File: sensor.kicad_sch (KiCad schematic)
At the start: 7 parts, among them U1 MAXM86161EFD+T

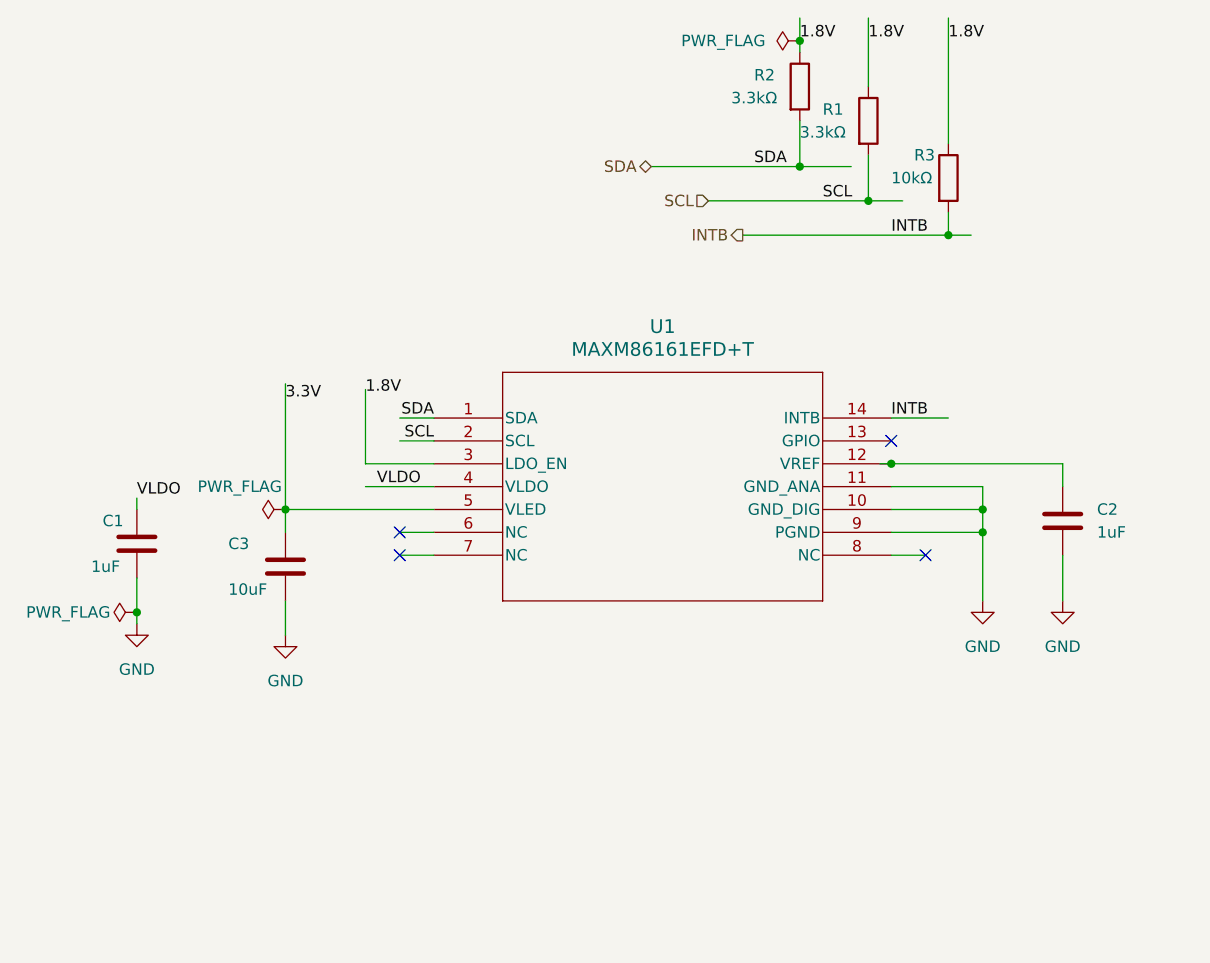
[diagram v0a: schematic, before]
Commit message: first finished schematic version of the MCU as well as sensor. starting out with schematic of the power related components
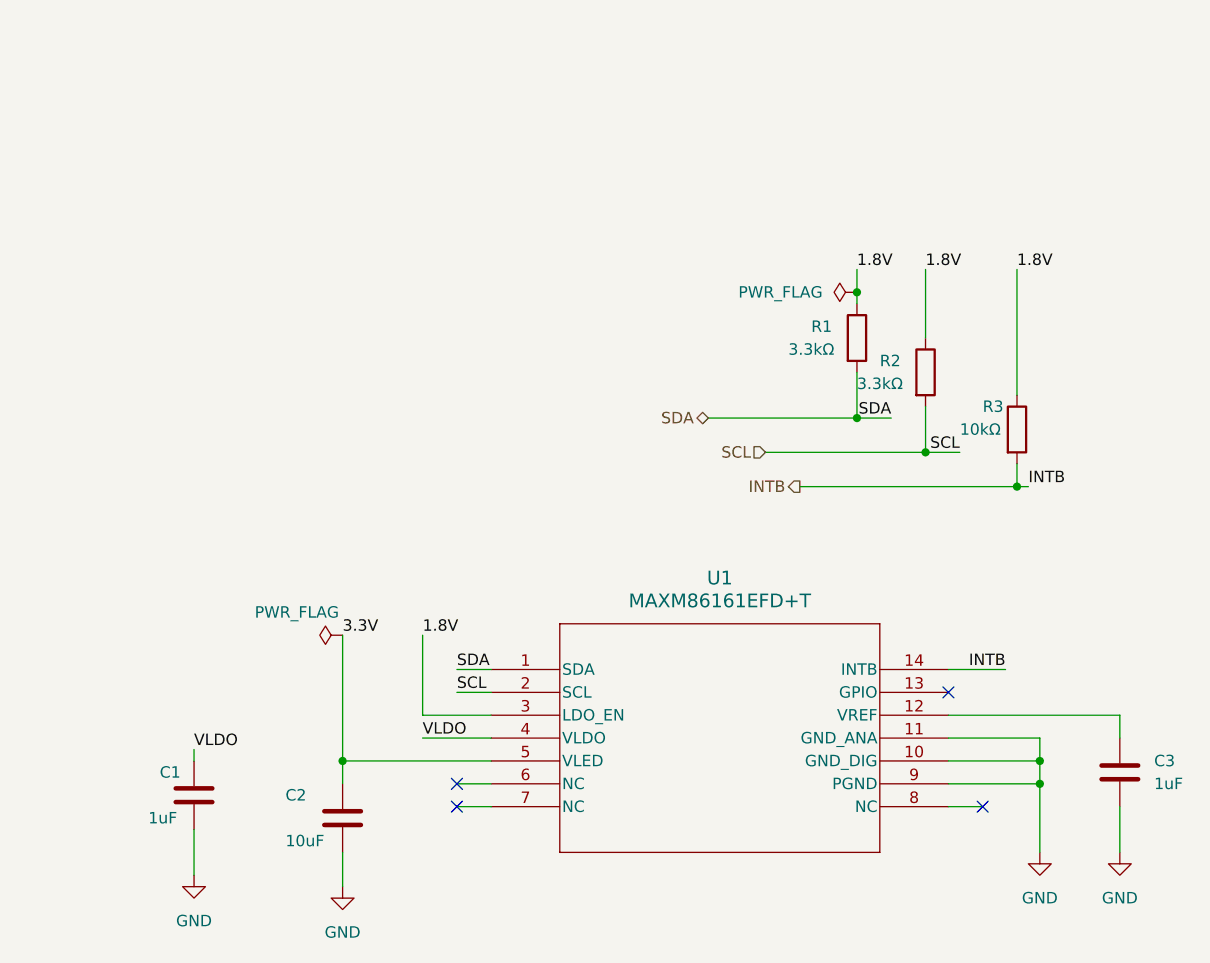
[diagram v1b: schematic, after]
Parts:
- C2: value 1uF -> 10uF
- C3: value 10uF -> 1uF
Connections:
- net 3.3V: now also C2.1; no longer C3.1
- net SCL: now also R2.2; no longer R1.2
- net SDA: now also R1.2; no longer R2.2
- net at U1.12 (VREF): now also C3.1; no longer C2.1

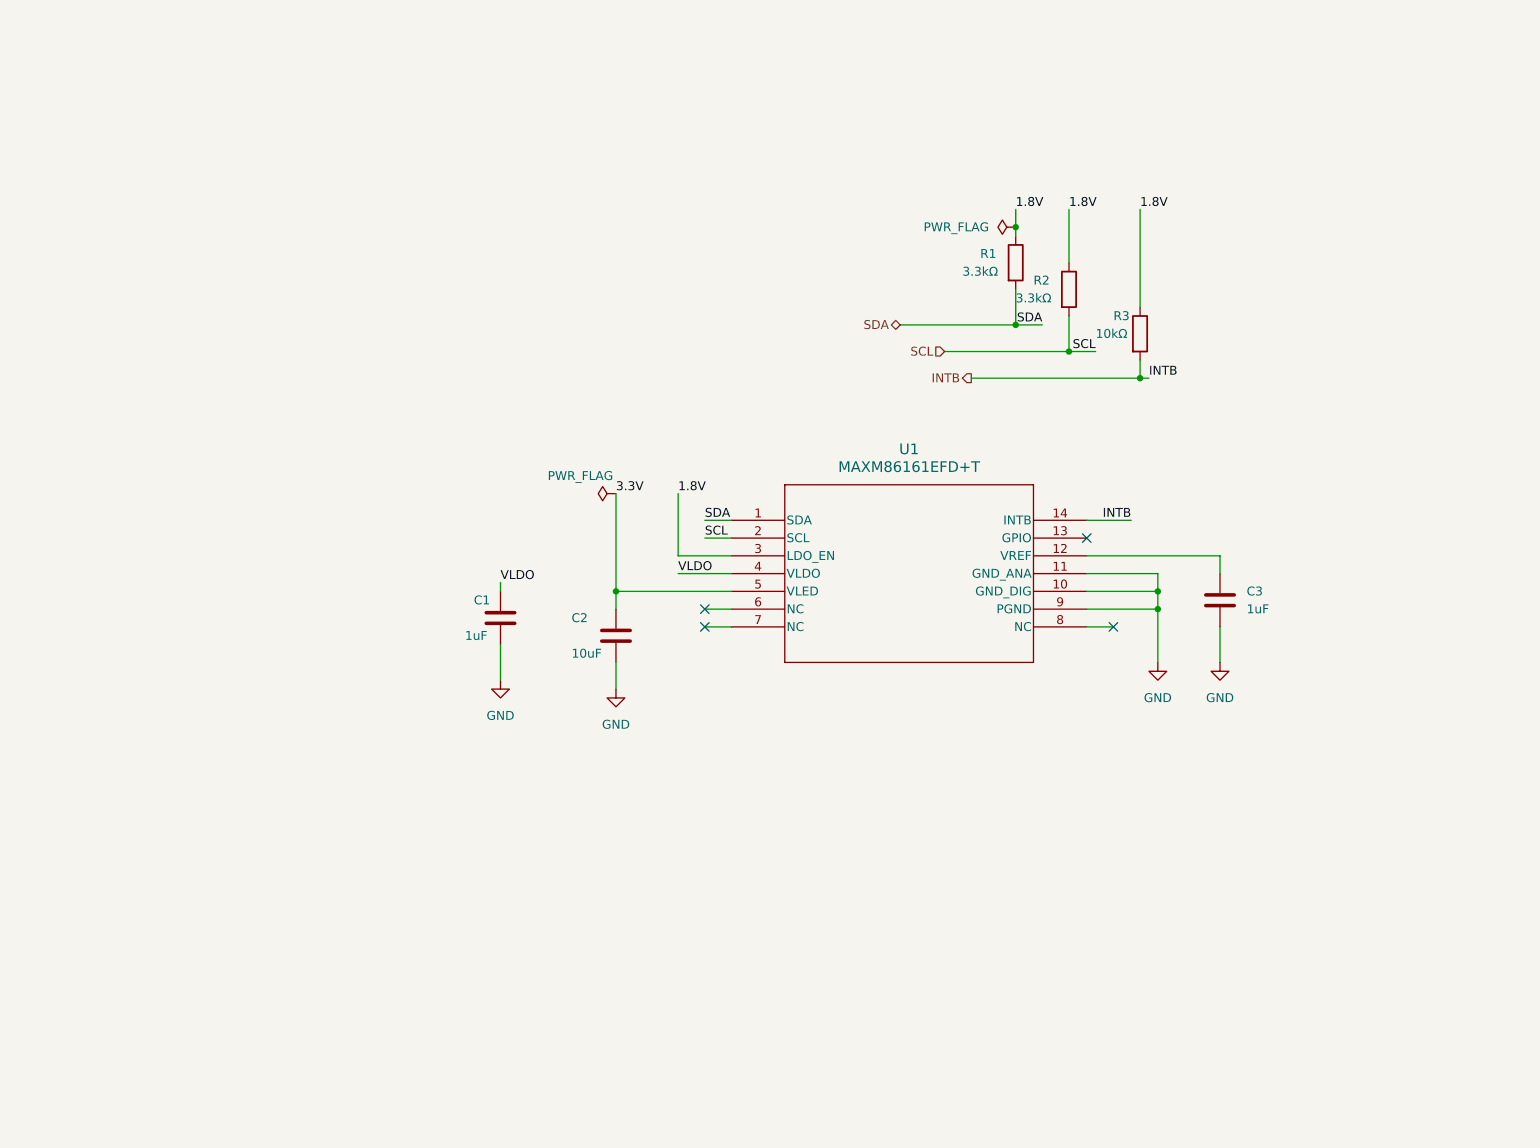
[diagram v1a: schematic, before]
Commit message: done with first version PowerSection of LoTiBloxy plus MCU plus sensor sheets. still have to add meaningfull comments to all schematic components. still have to make sure every symbol is associated to footprint. still have to perform ERC on what implemented.
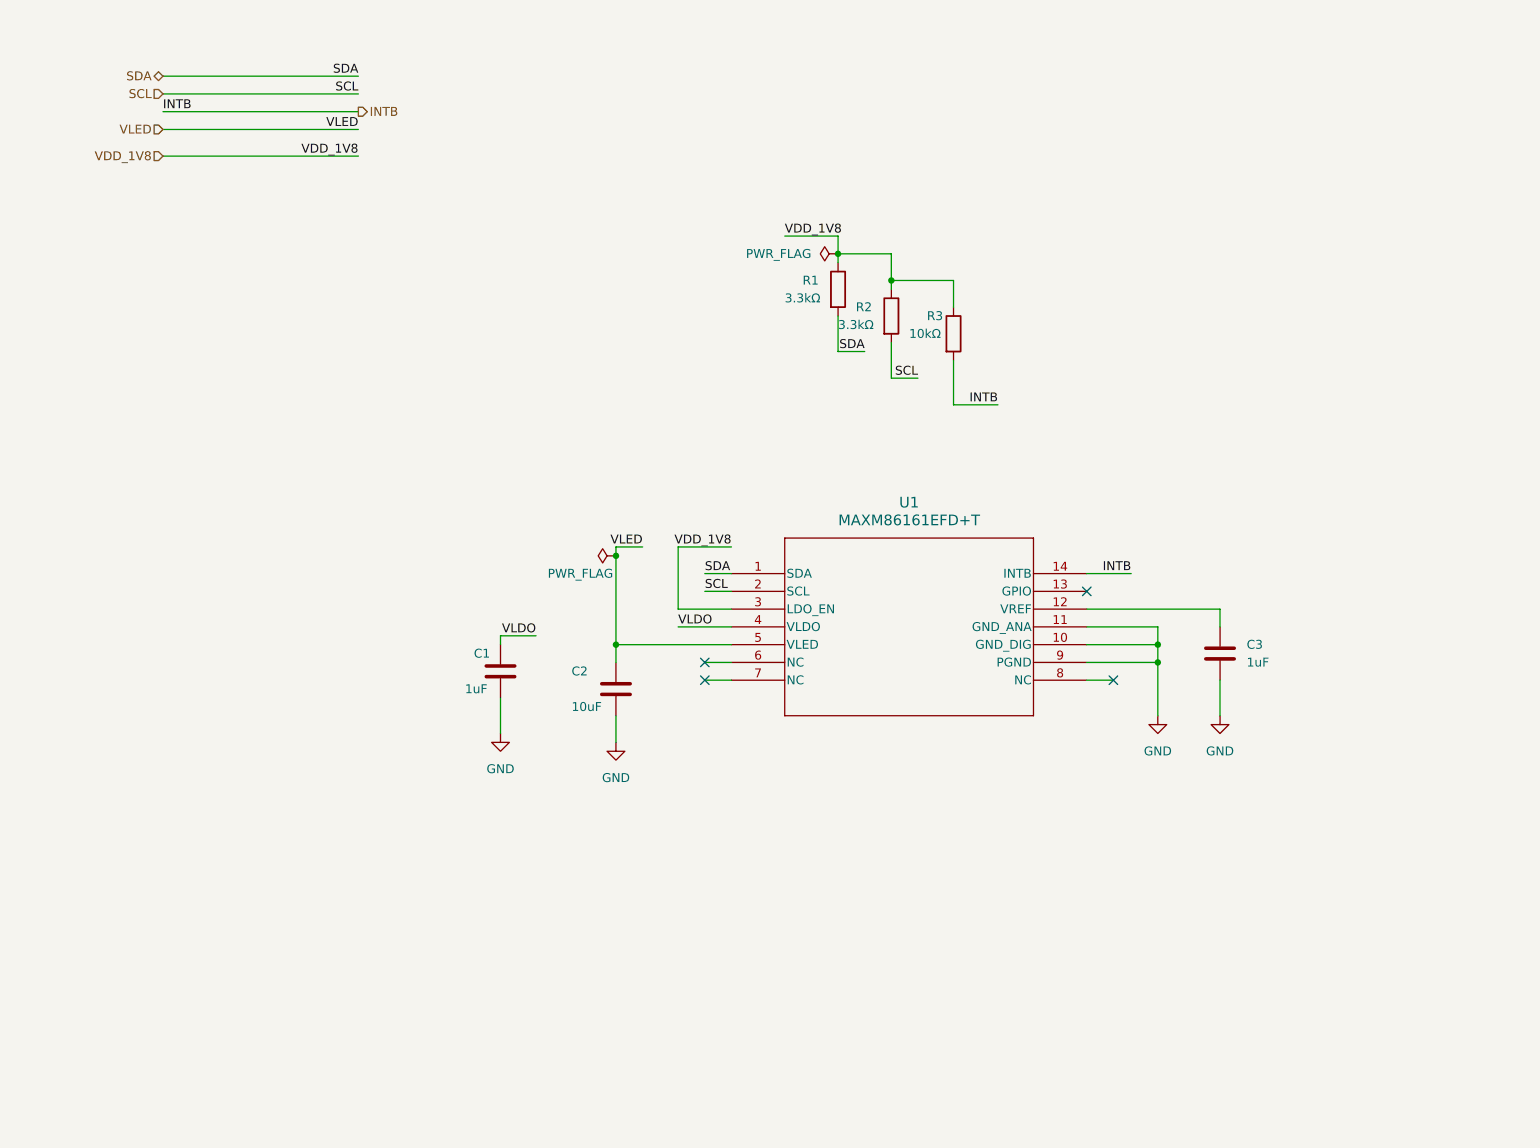
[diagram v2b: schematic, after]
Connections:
- net 1.8V renamed VDD_1V8
- net 3.3V renamed VLED
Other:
- moved on the sheet: C1, C2, C3, R1, R2, R3, U1

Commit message: finished associating each component of each sheet of schematic to relative footprint. filled in first version field for BOM. Provided organized hierechical level directories for all the datasheets for each used component.
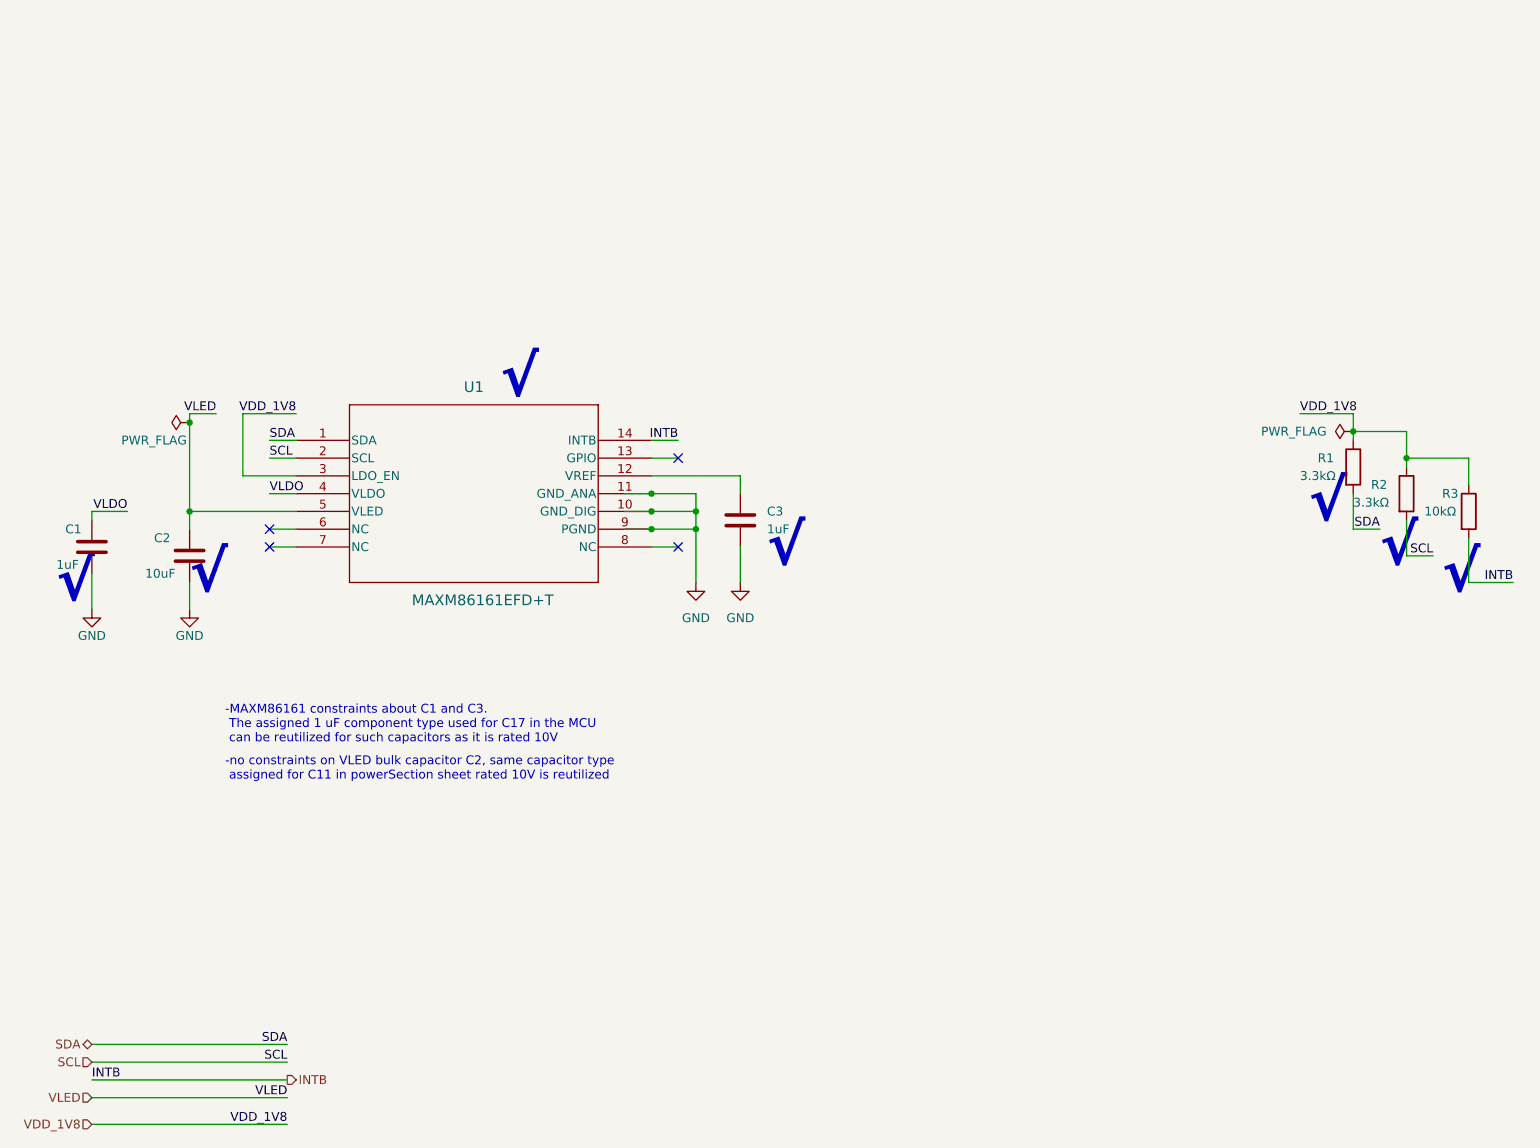
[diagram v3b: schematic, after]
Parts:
- C1, C3: footprint Capacitor_SMD_local:C_0603_1608Metric -> Capacitor_SMD_local:C_0402_1005Metric; MANUFACTURER (none) -> YAGEO; MPN (none) -> CC0402KRX5R6BB105; Package (none) -> 0402; Price (none) -> 0.09; mounting type (none) -> SMD; rohs (none) -> yes; vendor (none) -> DigiKey; vendor part number (none) -> 311-1439-1-ND
- C2: MANUFACTURER (none) -> Murata Electronics; MPN (none) -> GRM188R60J106ME47D; Package (none) -> 0603; Price (none) -> 0.10; mounting type (none) -> SMD; rohs (none) -> yes; vendor (none) -> DigiKey; vendor part number (none) -> 490-3896-1-ND
- R1, R2: footprint Resistor_SMD_local:R_0603_1608Metric -> Resistor_SMD_local:R_0402_1005Metric; MANUFACTURER (none) -> Stackpole Electronics Inc; MPN (none) -> RMCF0402FT3K30; Package (none) -> 0402; Price (none) -> 0.09; mounting type (none) -> SMD; rohs (none) -> yes; vendor (none) -> DigiKey; vendor part number (none) -> RMCF0402FT3K30CT-ND
- R3: footprint Resistor_SMD_local:R_0603_1608Metric -> Resistor_SMD_local:R_0402_1005Metric; MANUFACTURER (none) -> Stackpole Electronics Inc; MPN (none) -> RMCF0402FT10K0; Package (none) -> 0402; Price (none) -> 0.09; mounting type (none) -> SMD; rohs (none) -> yes; vendor (none) -> DigiKey; vendor part number (none) -> RMCF0402FT10K0CT-ND
- U1: MANUFACTURER (none) -> Analog Devices Inc./Maxim Integrated; MPN (none) -> MAXM86161EFD+T; Package (none) -> -; Price (none) -> 8.95; mounting type (none) -> SMD; rohs (none) -> yes; vendor (none) -> DigiKey; vendor part number (none) -> 175-MAXM86161EFD+TCT-ND
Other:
- note added: "-MAXM86161 constraints about C1 and C3. The assigned 1 uF component type used for C17 in the MCU can be reutilized for such capacitors as it is rated 10V"
- note added: "-no constraints on VLED bulk capacitor C2, same capacitor type assigned for C11 in powerSection sheet rated 10V is reutilized"
- note added: "√"
- moved on the sheet: C1, C2, C3, R1, R2, R3, U1

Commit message: ERC step done. most important errors and warnings resolved (the ones about unspecified pins etcetra). with the occasion have done also the checking of the symbols of each component to make sure of correct type of pins.have assigned the different fields related to the first BOM to all the components. need to still assign data sheets and description fields for some components
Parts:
- C1, C3, R1, R2, R3: Price 0.09 -> 0.09 €
- C2: Price 0.10 -> 0.10 €
- U1: Price 8.95 -> 8.95 €
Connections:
- net VREF: now reaches C3.1, U1.12 (VREF)
